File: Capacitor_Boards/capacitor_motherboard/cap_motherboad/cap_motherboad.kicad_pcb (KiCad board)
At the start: 2 copper layers, 221.5 x 124 mm, 14 parts, among them J1 Conn_01x02_Female, J10 Conn_01x02_Female, J11 Conn_01x02_Female, J12 Conn_01x02_Female, J2 Conn_01x02_Female, J3 Conn_01x02_Female, J4 Conn_01x02_Female, J5 Conn_01x02_Female, J6 Conn_01x02_Female, J7 Conn_01x02_Female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

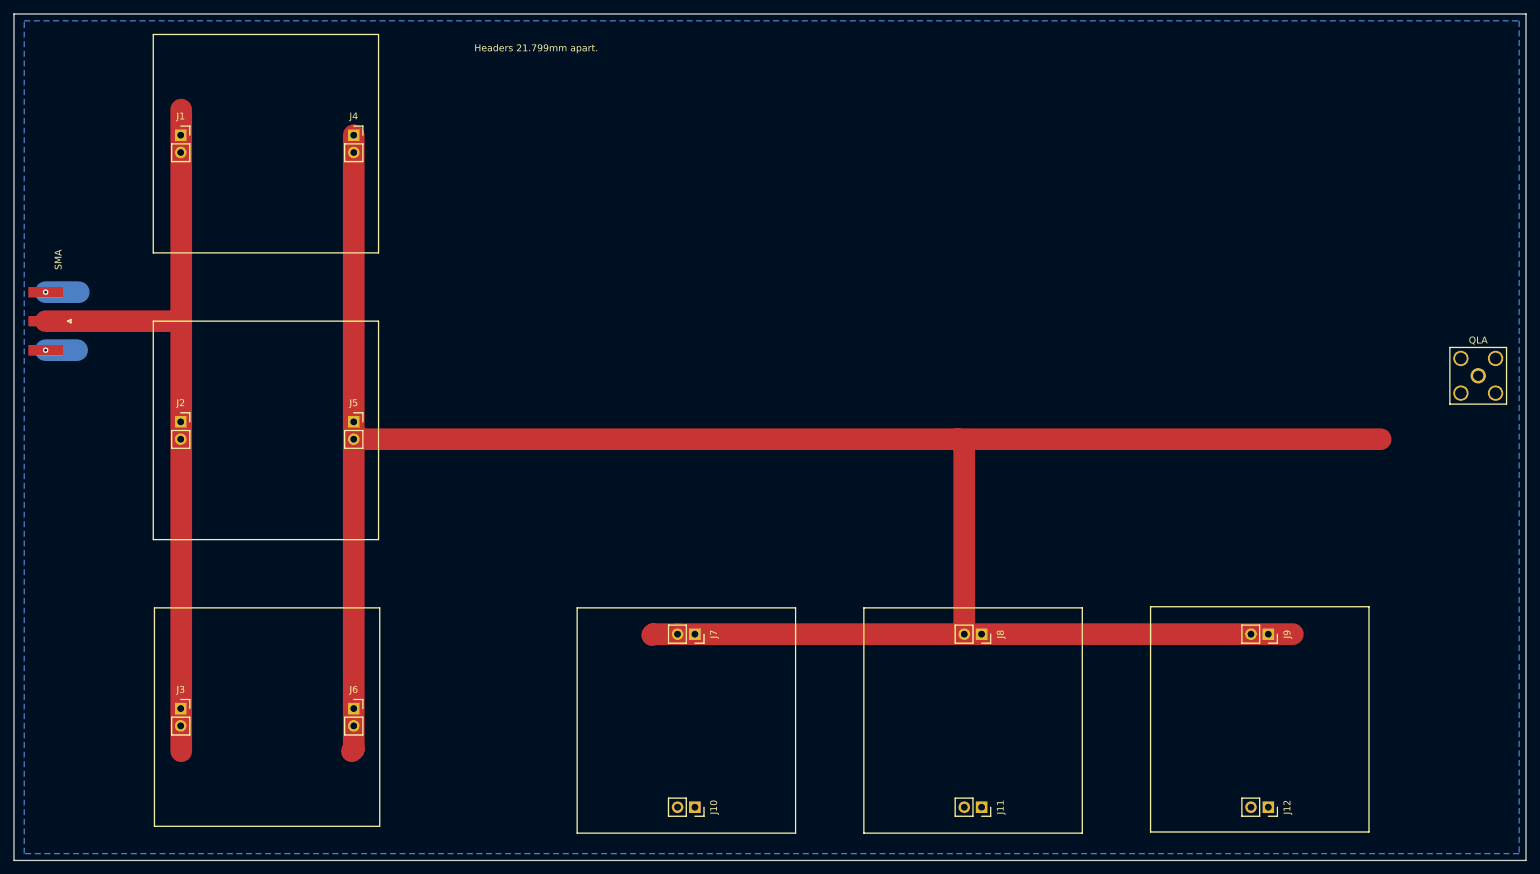
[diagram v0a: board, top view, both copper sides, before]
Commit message: resized capacitor daughterboard to have just 2 caps.
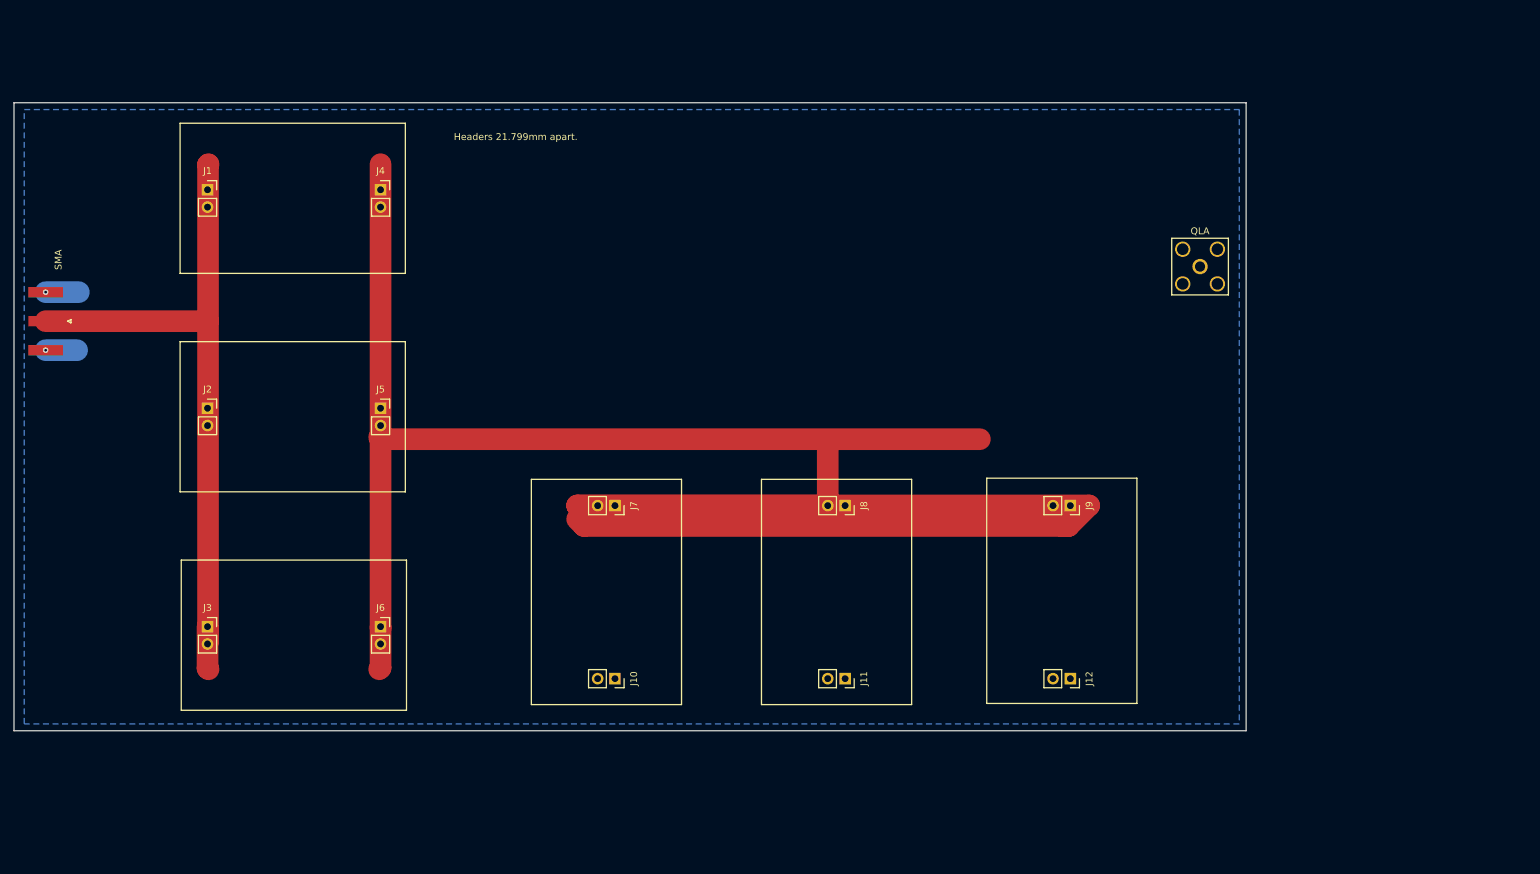
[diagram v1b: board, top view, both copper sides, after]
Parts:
- moved QLA 43.8 mm to (203.2, 62.0)
- moved J12 34.6 mm to (184.2, 122.4)
- moved J9 34.6 mm to (184.2, 97.0)
- moved J11 27.5 mm to (151.2, 122.4)
- moved J8 27.5 mm to (151.2, 97.0)
- moved J10 22.2 mm to (117.5, 122.4)
- moved J7 22.2 mm to (117.5, 97.0)
- moved J3 12.6 mm to (57.9, 114.8)
- moved J6 12.6 mm to (83.2, 114.8)
- moved J1 8.91 mm to (57.9, 50.8)
- moved J4 8.91 mm to (83.2, 50.8)
- moved J2 4.41 mm to (57.9, 82.8)
- moved J5 4.41 mm to (83.2, 82.8)
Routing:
- net Net-(J1-Pad1): track 113.9 -> 100.1 mm
- net Net-(J4-Pad1): track 363.7 -> 359.6 mm
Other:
- board size 221.5 x 124 mm -> 180.5 x 92 mm
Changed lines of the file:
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@@
   (net 3 "Net-(J1-Pad1)")
   (footprint "Connector_PinSocket_2.54mm:PinSocket_1x02_P2.54mm_Vertical" (layer "F.Cu")
-    (at 53.9255 84.75)
+    (at 57.8505 82.75)
     (descr "Through hole straight socket strip, 1x02, 2.54mm pitch, single row (from Kicad 4.0.7), script generated")
     (tags "Through hole socket strip THT 1x02 2.54mm single row")
@@
   )
   (footprint "Connector_PinSocket_2.54mm:PinSocket_1x02_P2.54mm_Vertical" (layer "F.Cu")
-    (at 213.25 141.1995 -90)
+    (at 184.25 122.3695 -90)
     (descr "Through hole straight socket strip, 1x02, 2.54mm pitch, single row (from Kicad 4.0.7), script generated")
     (tags "Through hole socket strip THT 1x02 2.54mm single row")
@@
   )
   (footprint "Connector_PinSocket_2.54mm:PinSocket_1x02_P2.54mm_Vertical" (layer "F.Cu")
-    (at 79.27414 126.75)
+    (at 83.19914 114.75)
     (descr "Through hole straight socket strip, 1x02, 2.54mm pitch, single row (from Kicad 4.0.7), script generated")
     (tags "Through hole socket strip THT 1x02 2.54mm single row")
@@
   )
   (footprint "Connector_PinSocket_2.54mm:PinSocket_1x02_P2.54mm_Vertical" (layer "F.Cu")
-    (at 53.9255 126.75)
+    (at 57.8505 114.75)
     (descr "Through hole straight socket strip, 1x02, 2.54mm pitch, single row (from Kicad 4.0.7), script generated")
     (tags "Through hole socket strip THT 1x02 2.54mm single row")
@@
   )
   (footprint "Connector_PinSocket_2.54mm:PinSocket_1x02_P2.54mm_Vertical" (layer "F.Cu")
-    (at 53.9255 42.75)
+    (at 57.8505 50.75)
     (descr "Through hole straight socket strip, 1x02, 2.54mm pitch, single row (from Kicad 4.0.7), script generated")
     (tags "Through hole socket strip THT 1x02 2.54mm single row")
@@
   )
   (footprint "Connector_PinSocket_2.54mm:PinSocket_1x02_P2.54mm_Vertical" (layer "F.Cu")
-    (at 79.27414 42.75)
+    (at 83.19914 50.75)
     (descr "Through hole straight socket strip, 1x02, 2.54mm pitch, single row (from Kicad 4.0.7), script generated")
     (tags "Through hole socket strip THT 1x02 2.54mm single row")
@@
   )
   (footprint "Connector_PinSocket_2.54mm:PinSocket_1x02_P2.54mm_Vertical" (layer "F.Cu")
-    (at 213.25 115.8505 -90)
+    (at 184.25 97.0205 -90)
     (descr "Through hole straight socket strip, 1x02, 2.54mm pitch, single row (from Kicad 4.0.7), script generated")
     (tags "Through hole socket strip THT 1x02 2.54mm single row")
@@
   )
   (footprint "Connector_PinSocket_2.54mm:PinSocket_1x02_P2.54mm_Vertical" (layer "F.Cu")
-    (at 129.25 141.1995 -90)
+    (at 117.54 122.3695 -90)
     (descr "Through hole straight socket strip, 1x02, 2.54mm pitch, single row (from Kicad 4.0.7), script generated")
     (tags "Through hole socket strip THT 1x02 2.54mm single row")
@@
   )
   (footprint "Connector_PinSocket_2.54mm:PinSocket_1x02_P2.54mm_Vertical" (layer "F.Cu")
-    (at 79.27414 84.75)
+    (at 83.19914 82.75)
     (descr "Through hole straight socket strip, 1x02, 2.54mm pitch, single row (from Kicad 4.0.7), script generated")
     (tags "Through hole socket strip THT 1x02 2.54mm single row")
@@
   )
   (footprint "Connector_PinSocket_2.54mm:PinSocket_1x02_P2.54mm_Vertical" (layer "F.Cu")
-    (at 171.25 141.1995 -90)
+    (at 151.25 122.3695 -90)
     (descr "Through hole straight socket strip, 1x02, 2.54mm pitch, single row (from Kicad 4.0.7), script generated")
     (tags "Through hole socket strip THT 1x02 2.54mm single row")
@@
   )
   (footprint "Connector_PinSocket_2.54mm:PinSocket_1x02_P2.54mm_Vertical" (layer "F.Cu")
-    (at 171.25 115.8505 -90)
+    (at 151.25 97.0205 -90)
     (descr "Through hole straight socket strip, 1x02, 2.54mm pitch, single row (from Kicad 4.0.7), script generated")
     (tags "Through hole socket strip THT 1x02 2.54mm single row")
@@
   )
   (footprint "Connector_PinSocket_2.54mm:PinSocket_1x02_P2.54mm_Vertical" (layer "F.Cu")
-    (at 129.25 115.8505 -90)
+    (at 117.54 97.0205 -90)
     (descr "Through hole straight socket strip, 1x02, 2.54mm pitch, single row (from Kicad 4.0.7), script generated")
     (tags "Through hole socket strip THT 1x02 2.54mm single row")
@@
   )
   (footprint "Connector_Coaxial:SMA_Amphenol_132203-12_Horizontal" (layer "F.Cu")
-    (at 244 78 -90)
+    (at 203.25 62 -90)
     (descr "https://www.amphenolrf.com/media/downloads/1769/132203-12.pdf")
     (tags "SMA THT Female Jack Horizontal")
@@
     )
   )
-  (gr_rect (start 196 144.83) (end 228 111.83) (layer "F.SilkS") (width 0.15) (fill none))
-  (gr_rect (start 50.075 112) (end 83.075 144) (layer "F.SilkS") (width 0.15) (fill none))
-  (gr_rect (start 112 145) (end 144 112) (layer "F.SilkS") (width 0.15) (fill none))
-  (gr_rect (start 154 145) (end 186 112) (layer "F.SilkS") (width 0.15) (fill none))
-  (gr_rect (start 49.905 28) (end 82.905 60) (layer "F.SilkS") (width 0.15) (fill none))
-  (gr_rect (start 49.905 70) (end 82.905 102) (layer "F.SilkS") (width 0.15) (fill none))
-  (gr_rect (start 29.5 25) (end 251 149) (layer "Edge.Cuts") (width 0.1) (fill none))
-  (gr_text "Headers 21.799mm apart." (at 106 30) (layer "F.SilkS")
+  (gr_rect (start 172 126) (end 194 93) (layer "F.SilkS") (width 0.15) (fill none))
+  (gr_rect (start 54 105) (end 87 127) (layer "F.SilkS") (width 0.15) (fill none))
+  (gr_rect (start 105.29 126.17) (end 127.29 93.17) (layer "F.SilkS") (width 0.15) (fill none))
+  (gr_rect (start 139 126.17) (end 161 93.17) (layer "F.SilkS") (width 0.15) (fill none))
+  (gr_rect (start 53.83 41) (end 86.83 63) (layer "F.SilkS") (width 0.15) (fill none))
+  (gr_rect (start 53.83 73) (end 86.83 95) (layer "F.SilkS") (width 0.15) (fill none))
+  (gr_rect (start 29.5 38) (end 210 130) (layer "Edge.Cuts") (width 0.1) (fill none))
+  (gr_text "Headers 21.799mm apart." (at 103 43) (layer "F.SilkS")
     (effects (font (size 1 1) (thickness 0.15)))
   )
-  (segment (start 126.71 115.8505) (end 216.8505 115.8505) (width 3.175) (layer "F.Cu") (net 1))
-  (segment (start 79.27414 132.72586) (end 79 133) (width 3.175) (layer "F.Cu") (net 1))
-  (segment (start 123.1495 115.8505) (end 123 116) (width 3.175) (layer "F.Cu") (net 1))
-  (segment (start 168.71 88.29) (end 167.71 87.29) (width 3.175) (layer "F.Cu") (net 1))
-  (segment (start 126.71 115.8505) (end 123.1495 115.8505) (width 3.175) (layer "F.Cu") (net 1))
-  (segment (start 79.27414 87.29) (end 167.71 87.29) (width 3.175) (layer "F.Cu") (net 1))
-  (segment (start 167.71 87.29) (end 229.71 87.29) (width 3.175) (layer "F.Cu") (net 1))
-  (segment (start 168.71 115.8505) (end 168.71 88.29) (width 3.175) (layer "F.Cu") (net 1))
-  (segment (start 79.27414 42.75) (end 79.27414 132.72586) (width 3.175) (layer "F.Cu") (net 1))
+  (segment (start 184 100) (end 183 100) (width 3.175) (layer "F.Cu") (net 1))
+  (segment (start 83.19914 120.80086) (end 83 121) (width 3.175) (layer "F.Cu") (net 1))
+  (segment (start 148.71 97.0205) (end 112.0205 97.0205) (width 3.175) (layer "F.Cu") (net 1))
+  (segment (start 187 97) (end 184 100) (width 3.175) (layer "F.Cu") (net 1))
+  (segment (start 83 87) (end 83.29 87.29) (width 3.175) (layer "F.Cu") (net 1))
+  (segment (start 83.19914 114.75) (end 83.19914 120.80086) (width 3.175) (layer "F.Cu") (net 1))
+  (segment (start 83.19914 47) (end 83.19914 115) (width 3.175) (layer "F.Cu") (net 1))
+  (segment (start 112.0205 97.0205) (end 112 97) (width 3.175) (layer "F.Cu") (net 1))
+  (segment (start 183 100) (end 113 100) (width 3.175) (layer "F.Cu") (net 1))
+  (segment (start 113 100) (end 112 99) (width 3.175) (layer "F.Cu") (net 1))
+  (segment (start 83.29 87.29) (end 171 87.29) (width 3.175) (layer "F.Cu") (net 1))
+  (segment (start 112 97) (end 187 97) (width 3.175) (layer "F.Cu") (net 1))
+  (segment (start 148.71 97.0205) (end 148.71 88.29) (width 3.175) (layer "F.Cu") (net 1))
   (via (at 34.1375 74.25) (size 0.8) (drill 0.4) (layers "F.Cu" "B.Cu") (net 2))
   (via (at 34.1375 65.75) (size 0.8) (drill 0.4) (layers "F.Cu" "B.Cu") (remove_unused_layers) (keep_end_layers) (net 2))
   (segment (start 34.1375 65.75) (end 39 65.75) (width 3.175) (layer "B.Cu") (net 2))
   (segment (start 34.1375 74.25) (end 38.75 74.25) (width 3.175) (layer "B.Cu") (net 2))
-  (segment (start 54 70) (end 54 39) (width 3.175) (layer "F.Cu") (net 3))
-  (segment (start 34.1375 70) (end 54 70) (width 3.175) (layer "F.Cu") (net 3))
-  (segment (start 54 70) (end 54 133) (width 3.175) (layer "F.Cu") (net 3))
+  (segment (start 57.8505 120.8505) (end 58 121) (width 3.175) (layer "F.Cu") (net 3))
+  (segment (start 57.925 70) (end 57.925 117) (width 3.175) (layer "F.Cu") (net 3))
+  (segment (start 57.925 47.075) (end 57.925 70) (width 3.175) (layer "F.Cu") (net 3))
+  (segment (start 57.8505 114.75) (end 57.8505 120.8505) (width 3.175) (layer "F.Cu") (net 3))
+  (segment (start 34.1375 70) (end 57.925 70) (width 3.175) (layer "F.Cu") (net 3))
+  (segment (start 58 47) (end 57.925 47.075) (width 3.175) (layer "F.Cu") (net 3))
   (zone (net 2) (net_name "GND") (layer "B.Cu") (hatch edge 0.508)
     (connect_pads (clearance 0.508))
@@
     (polygon
       (pts
-        (xy 250 148)
-        (xy 31 148)
-        (xy 31 26)
-        (xy 250 26)
+        (xy 209 129)
+        (xy 31 129)
+        (xy 31 39)
+        (xy 209 39)
       )
     )
